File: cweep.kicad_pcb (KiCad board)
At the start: 2 copper layers, 105.2 x 82.3 mm, 38 parts

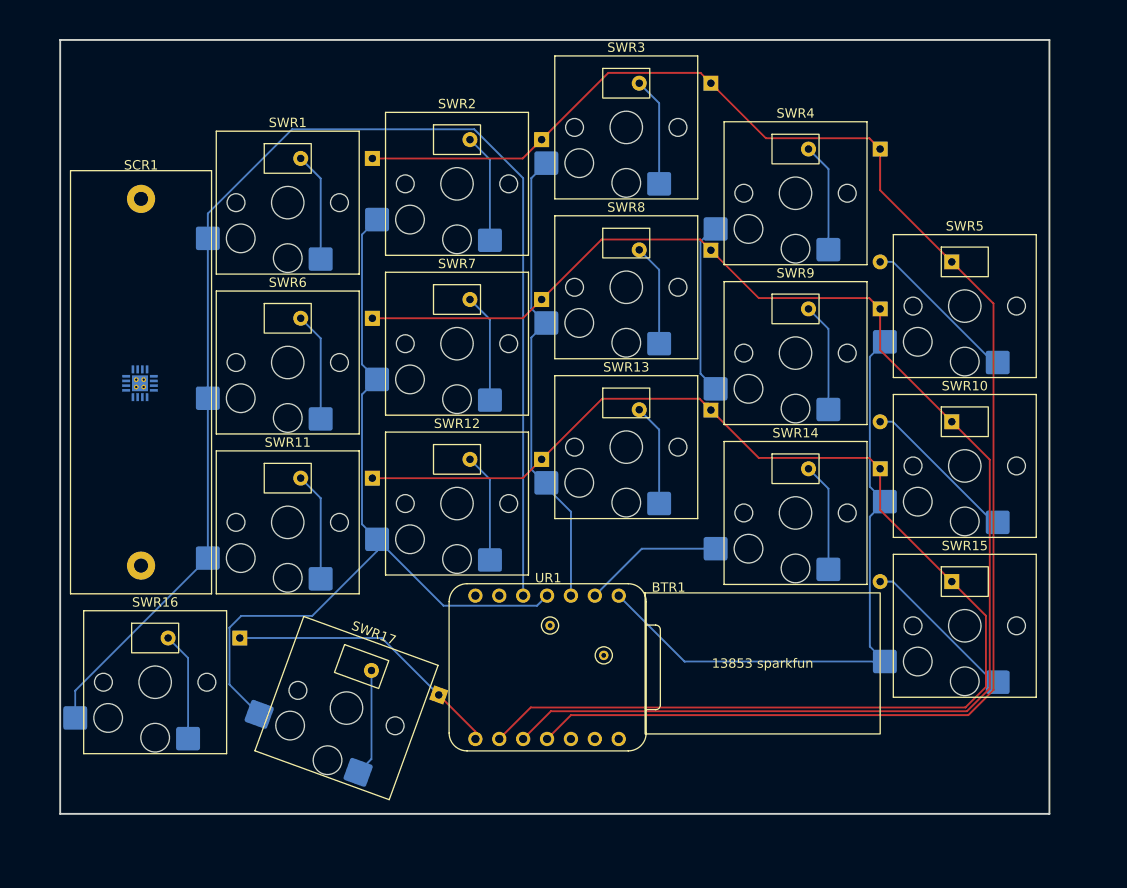
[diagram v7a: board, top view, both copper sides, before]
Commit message: fix: placement for key-cap tolerances
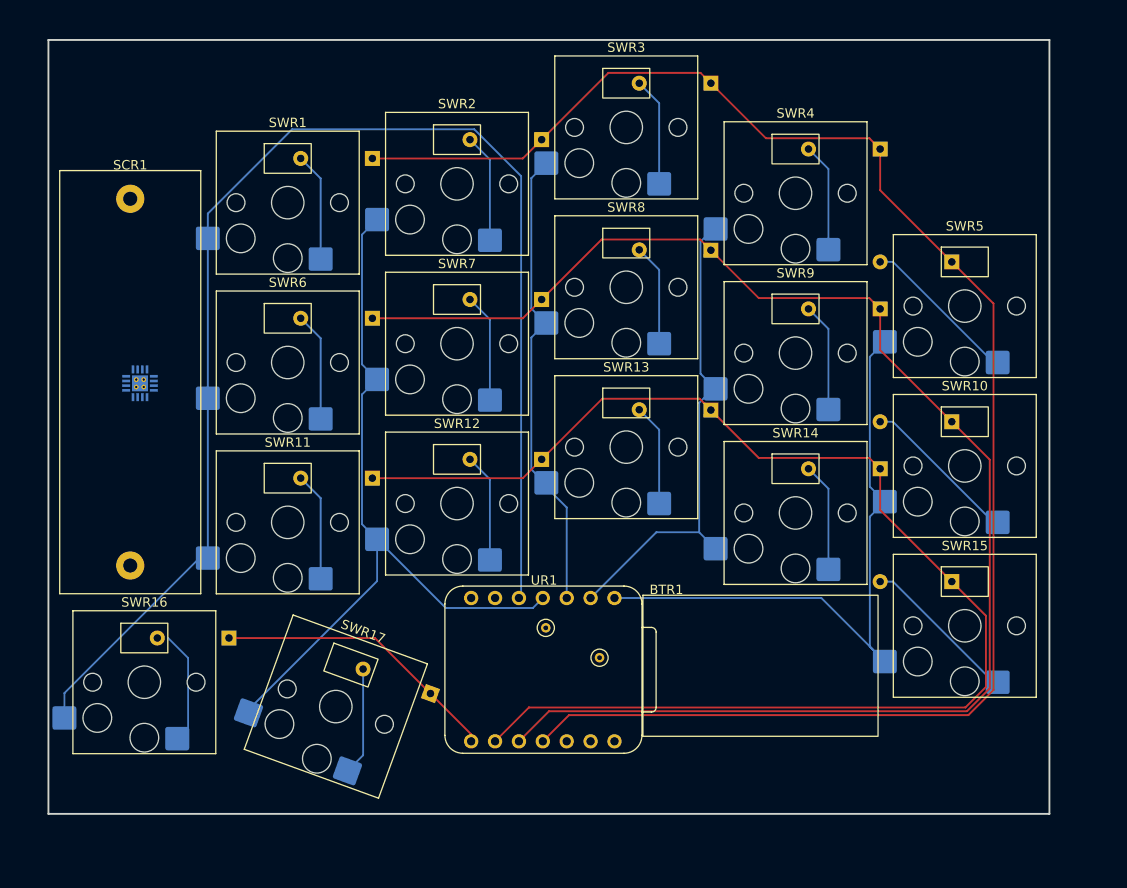
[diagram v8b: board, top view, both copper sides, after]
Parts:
- moved SCR1 1.15 mm to (162.4, 92.9)
- moved DR16 1.15 mm to (180.8, 97.3)
- moved SWR16 1.15 mm to (171.8, 102.0)
- moved SWR17 1.15 mm to (192.1, 104.6)
- moved DR17 0.90 mm to (202.2, 103.2)
- moved UR1 0.51 mm to (214.2, 100.8)
- moved BTR1 0.34 mm to (237.3, 100.2)
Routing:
- net /column r3: track 33.4 -> 51.5 mm
- net /column r1: track 88.9 -> 81.9 mm
- net /column r0: track 143.3 -> 144.5 mm
- net /row r3: track 30.0 -> 30.7 mm
- net /row r0: track 173.6 -> 174.2 mm
- net /row r2: track 142.5 -> 143.0 mm
- net /row r1: track 157.9 -> 158.5 mm
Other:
- board size 105.2 x 82.3 mm -> 106.4 x 82.3 mm
